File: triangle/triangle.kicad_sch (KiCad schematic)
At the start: 15 parts, among them J1 GND, J2 DIN, J3 5V, J4 GND, J5 DOUT, J6 5V, J7 GND, J8 DOUT, J9 5V

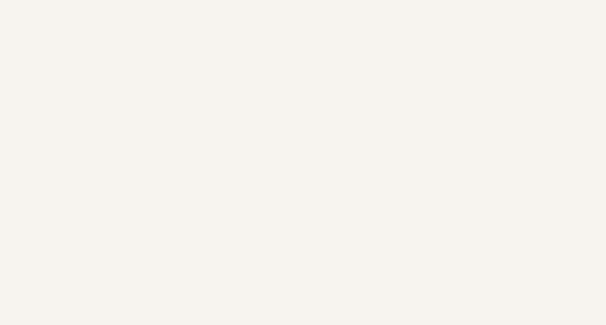
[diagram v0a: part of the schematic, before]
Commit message: Add tooling holes
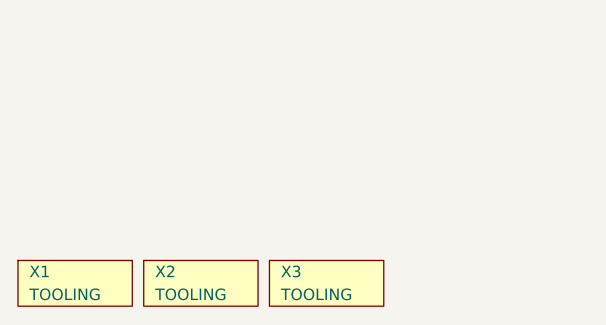
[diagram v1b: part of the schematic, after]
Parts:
- added X1, X2, X3: TOOLING, agg:M2.5_HOLE, symbol agg:PART
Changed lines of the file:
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@@
     (pin "1")
+  )
+  (symbol (lib_id "agg:PART") (at 19.05 190.5 0) (unit 1)
+    (in_bom yes) (on_board yes)
+    (property "Reference" "X1" (id 0) (at 20.32 187.96 0)
+      (effects (font (size 1.27 1.27)) (justify left))
+    )
+    (property "Value" "TOOLING" (id 1) (at 20.32 190.5 0)
+      (effects (font (size 1.27 1.27)) (justify left))
+    )
+    (property "Footprint" "agg:M2.5_HOLE" (id 2) (at 19.05 190.5 0)
+      (effects (font (size 1.27 1.27)) hide)
+    )
+    (property "Datasheet" "" (id 3) (at 19.05 190.5 0)
+      (effects (font (size 1.27 1.27)) hide)
+    )
+  )
+  (symbol (lib_id "agg:PART") (at 33.02 190.5 0) (unit 1)
+    (in_bom yes) (on_board yes)
+    (property "Reference" "X2" (id 0) (at 34.29 187.96 0)
+      (effects (font (size 1.27 1.27)) (justify left))
+    )
+    (property "Value" "TOOLING" (id 1) (at 34.29 190.5 0)
+      (effects (font (size 1.27 1.27)) (justify left))
+    )
+    (property "Footprint" "agg:M2.5_HOLE" (id 2) (at 33.02 190.5 0)
+      (effects (font (size 1.27 1.27)) hide)
+    )
+    (property "Datasheet" "" (id 3) (at 33.02 190.5 0)
+      (effects (font (size 1.27 1.27)) hide)
+    )
+  )
+  (symbol (lib_id "agg:PART") (at 46.99 190.5 0) (unit 1)
+    (in_bom yes) (on_board yes)
+    (property "Reference" "X3" (id 0) (at 48.26 187.96 0)
+      (effects (font (size 1.27 1.27)) (justify left))
+    )
+    (property "Value" "TOOLING" (id 1) (at 48.26 190.5 0)
+      (effects (font (size 1.27 1.27)) (justify left))
+    )
+    (property "Footprint" "agg:M2.5_HOLE" (id 2) (at 46.99 190.5 0)
+      (effects (font (size 1.27 1.27)) hide)
+    )
+    (property "Datasheet" "" (id 3) (at 46.99 190.5 0)
+      (effects (font (size 1.27 1.27)) hide)
+    )
   )
   (symbol (lib_id "agg:WS2812B-4020") (at 111.76 55.88 0) (unit 1)
@@
       (reference "LED3") (unit 1) (value "WS2812B-4020") (footprint "agg:WS2812B-4020")
     )
-  )
+    (path "/c13c7f00-fa78-4f7b-9e7d-0d70554cc7dc"
+      (reference "X1") (unit 1) (value "TOOLING") (footprint "agg:M2.5_HOLE")
+    )
+    (path "/351857dd-158d-4386-b05d-f7822a2600de"
+      (reference "X2") (unit 1) (value "TOOLING") (footprint "agg:M2.5_HOLE")
+    )
+    (path "/d62b2738-7058-4275-904e-75d95f099d17"
+      (reference "X3") (unit 1) (value "TOOLING") (footprint "agg:M2.5_HOLE")
+    )
+  )

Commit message: Update page info boxes
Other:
- title: (none) -> LEDEAF Triangle PCB
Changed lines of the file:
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@@
 (kicad_sch (version 20210406) (generator eeschema)
   (paper "A4")
+  (title_block
+    (title "LEDEAF Triangle PCB")
+    (date "2021-05-23")
+    (rev "1")
+    (comment 1 "Drawn By: AG")
+  )
   (junction (at 95.25 53.34) (diameter 0.9144) (color 0 0 0 0))
   (junction (at 95.25 71.12) (diameter 0.9144) (color 0 0 0 0))
